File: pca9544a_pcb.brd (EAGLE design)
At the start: 43 x 43 mm, 33 parts, among them IC1 PCA9544ABS

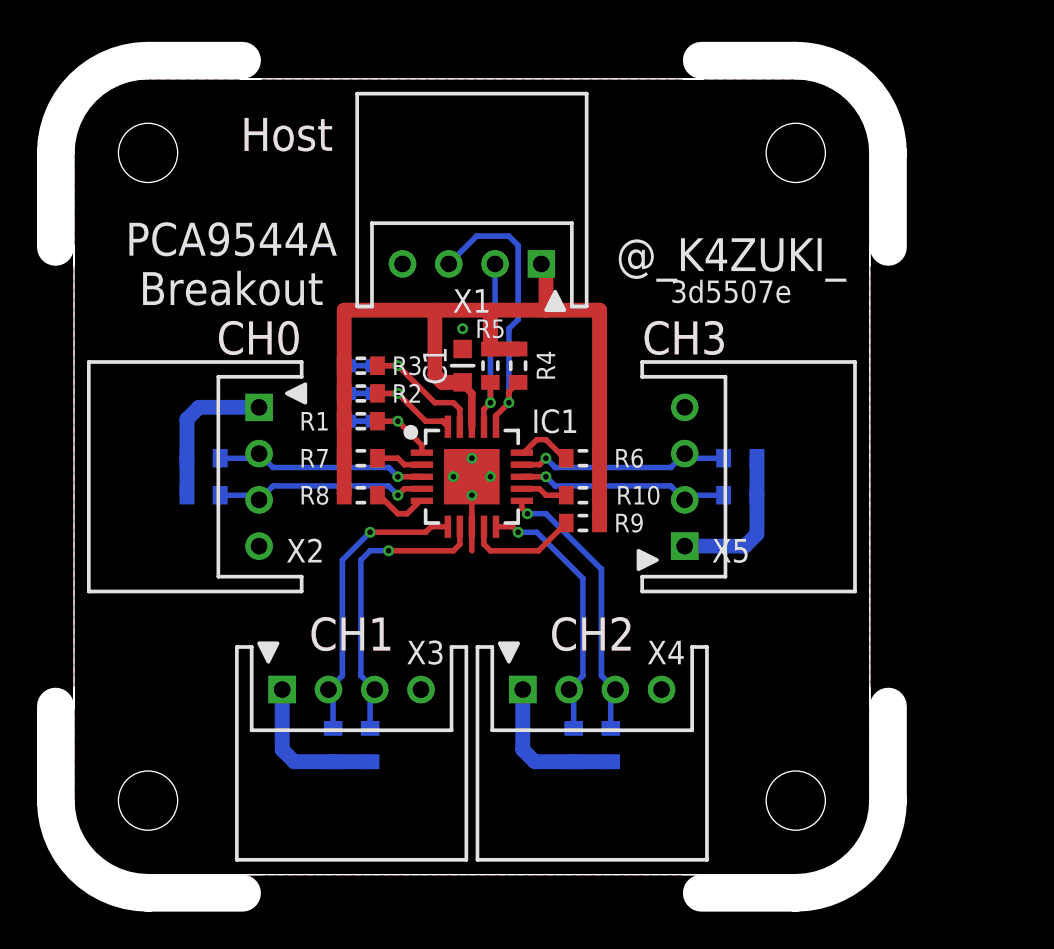
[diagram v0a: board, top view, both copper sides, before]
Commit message: add X6~X9 to short Host VDD and each channel VDD
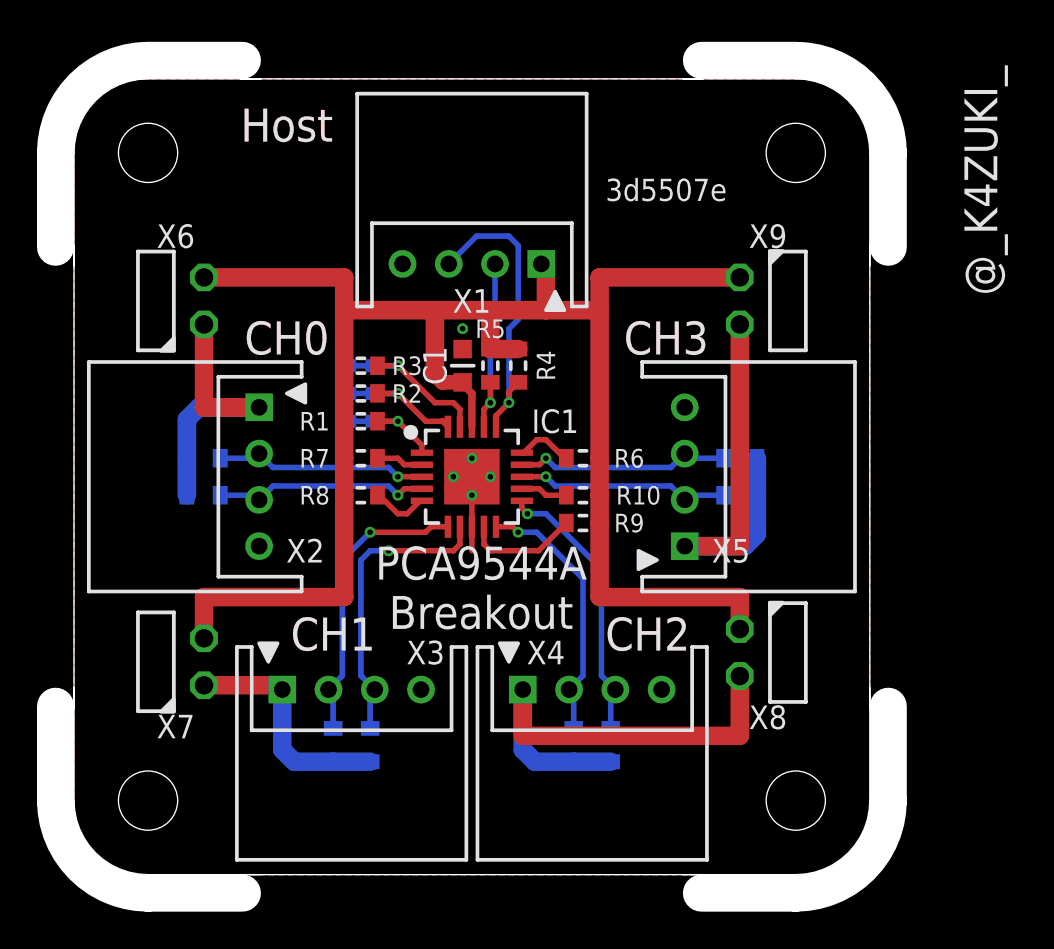
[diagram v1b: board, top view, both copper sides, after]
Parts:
- added X6, X7, X8, X9: TSW-102-02-S-S-RA, con-samtec.local:TSW-102-02-S-S-RA
- moved GIT1 6.52 mm to (32.0, 37.0)
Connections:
- net N$19: now also X6.1
- net N$20: now also X7.1
- net N$21: now also X8.2
- net N$22: now also X9.2
- net VCC: now also X6.2, X7.2, X8.1, X9.1
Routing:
- net VCC: track 49.4 -> 96.7 mm
- net N$21: track 8.27 -> 25.7 mm
- net N$22: track 8.27 -> 23.2 mm
- net N$19: track 8.27 -> 15.7 mm
- net N$20: track 8.27 -> 12.7 mm

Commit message: fix silk
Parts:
- GIT1: value 3d5507e -> 4bf204c
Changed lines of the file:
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@@
 <text x="31" y="13" size="1.778" layer="21" ratio="17" align="center">CH2</text>
 <text x="32" y="29" size="1.778" layer="21" ratio="17" align="center">CH3</text>
-<text x="49" y="37.5" size="1.778" layer="21" ratio="17" rot="R90" align="center">@_K4ZUKI_</text>
+<text x="35.5" y="35" size="1.778" layer="21" ratio="17" rot="R180" align="center">@_K4ZUKI_</text>
 <text x="22" y="15.5" size="1.778" layer="21" ratio="16" align="center">PCA9544A
 Breakout</text>
@@
 </autorouter>
 <elements>
-<element name="GIT1" library="git-revision" package="GIT-REVISION_1.2" value="3d5507e" x="32" y="37">
+<element name="GIT1" library="git-revision" package="GIT-REVISION_1.2" value="4bf204c" x="32" y="37">
 <attribute name="NOT_COMPONENT" value="YES" x="32" y="37" size="1.778" layer="27" display="off"/>
 </element>
@@
 </element>
 <element name="X9" library="con-samtec.local" package="TSW-102-02-S-S-RA" value="TSW-102-02-S-S-RA" x="37.5" y="31" smashed="yes" rot="R90">
-<attribute name="NAME" x="37.5" y="34.5" size="1.27" layer="25" ratio="16" rot="R180" align="center"/>
+<attribute name="NAME" x="41" y="28.5" size="1.27" layer="25" ratio="16" rot="R180" align="center"/>
 <attribute name="VALUE" x="44.5" y="35.4" size="1" layer="27" ratio="20" rot="R180"/>
 </element>

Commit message: gerber out
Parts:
- GIT1: value 4bf204c -> adf3d9e
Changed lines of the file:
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@@
 </autorouter>
 <elements>
-<element name="GIT1" library="git-revision" package="GIT-REVISION_1.2" value="4bf204c" x="32" y="37">
+<element name="GIT1" library="git-revision" package="GIT-REVISION_1.2" value="adf3d9e" x="32" y="37">
 <attribute name="NOT_COMPONENT" value="YES" x="32" y="37" size="1.778" layer="27" display="off"/>
 </element>
